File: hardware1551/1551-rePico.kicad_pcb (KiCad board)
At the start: 2 copper layers, 64.1 x 99.4 mm, 37 parts, among them J1 0.96_I2C_OLED, J10 TCBM, J11 JTAG, J6 Conn_01x05, J8 SD CARD, Q1 BSS138, Q2 BSS138, Q3 BSS138, Q4 BSS138, U1 Pico, U3 XC9572XL-VQ64, U4 6523 (pins), U5 6510T (pins), U6 6510T (socket for chip)

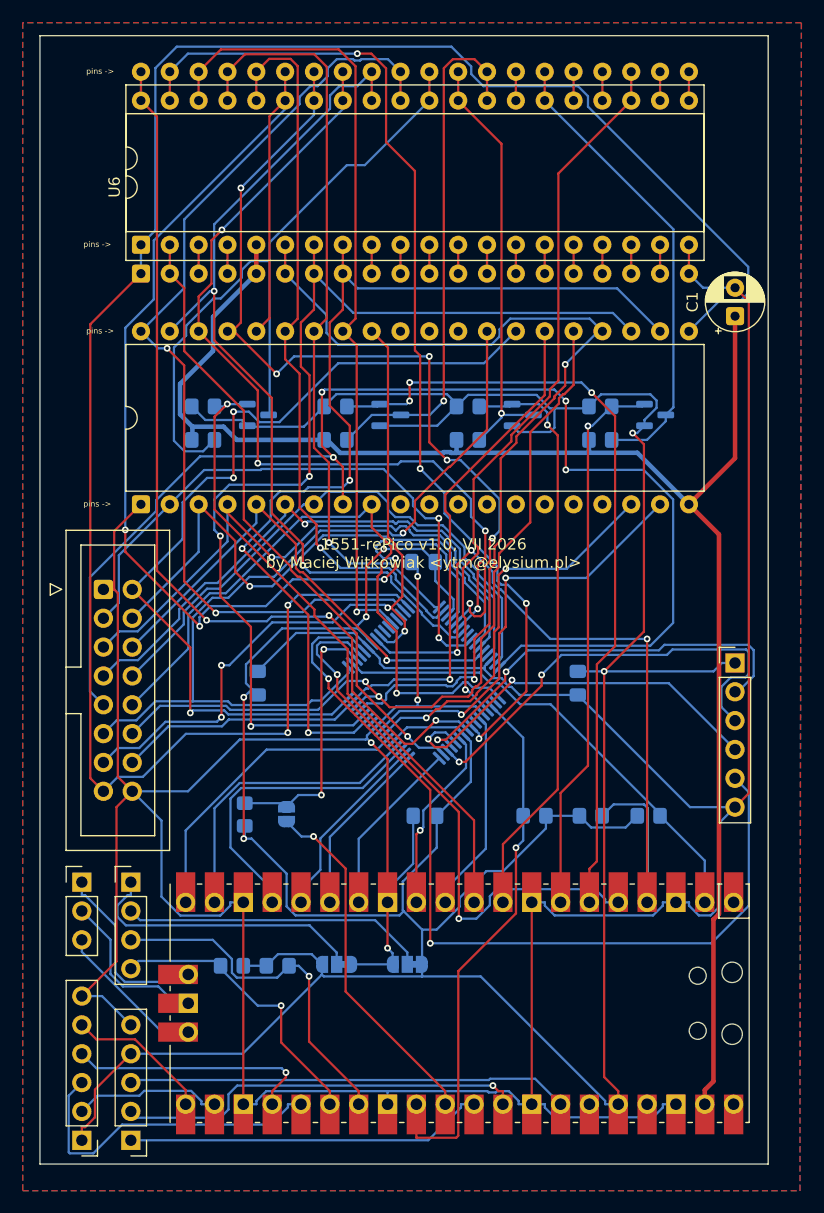
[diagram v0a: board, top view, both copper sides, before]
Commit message: jumpers for future GPIO0/GPIO3 experiments
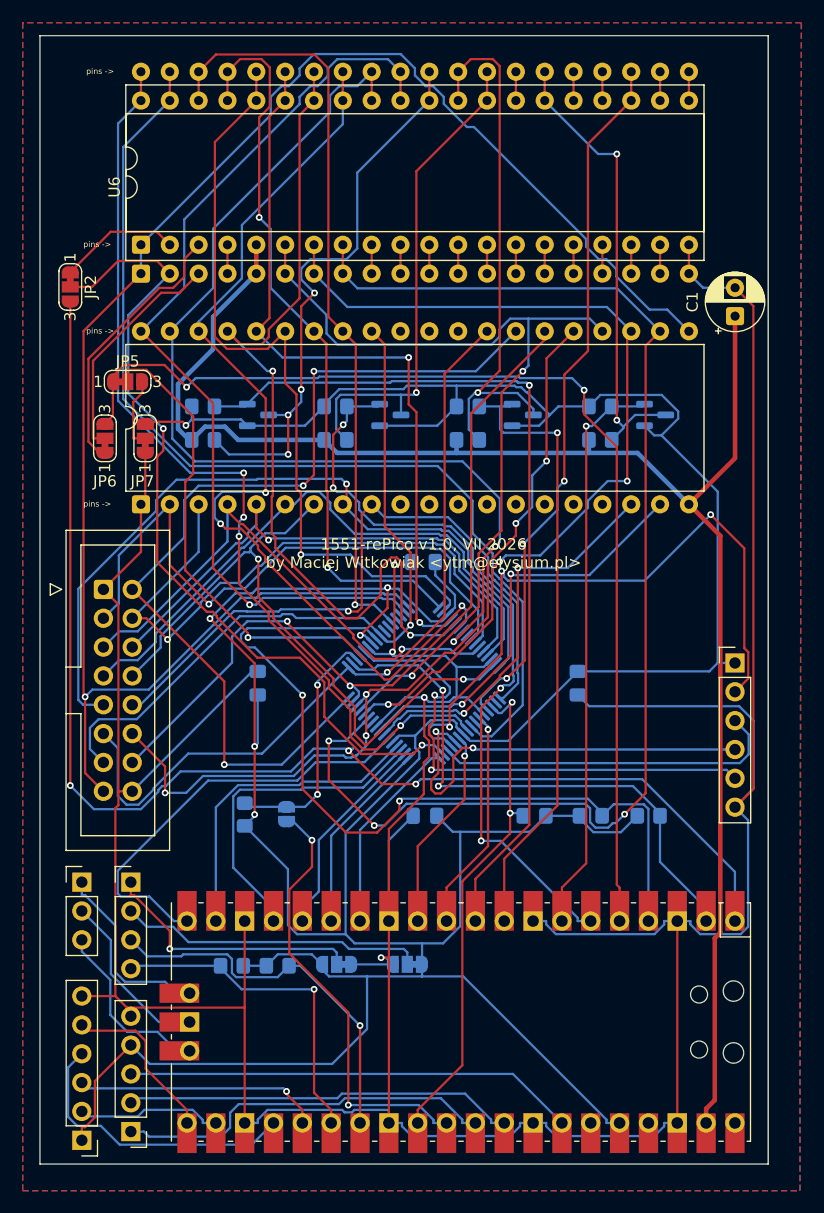
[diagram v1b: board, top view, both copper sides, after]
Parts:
- added JP2: SolderJumper_3_Bridged12, Jumper:SolderJumper-3_P1.3mm_Bridged12_RoundedPad1.0x1.5mm_NumberLabels, F.Cu at (100.8, 85.0)
- added JP5: SolderJumper_3_Bridged12, Jumper:SolderJumper-3_P1.3mm_Bridged12_RoundedPad1.0x1.5mm_NumberLabels, F.Cu at (105.9, 93.3)
- added JP6: SolderJumper_3_Bridged12, Jumper:SolderJumper-3_P1.3mm_Bridged12_RoundedPad1.0x1.5mm_NumberLabels, F.Cu at (103.9, 98.3)
- added JP7: SolderJumper_3_Bridged12, Jumper:SolderJumper-3_P1.3mm_Bridged12_RoundedPad1.0x1.5mm_NumberLabels, F.Cu at (107.4, 98.3)
- moved U1 1.66 mm to (135.2, 149.7)
- moved J6 0.76 mm to (106.1, 159.4)
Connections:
- U1 pad 1: unconnected-(U1-GPIO0-Pad1) -> Net-(JP2-B)
- U1 pad 5: /DEVNUM_3V3 -> Net-(JP5-A)
- U5 pad 2: /PHI0 -> /PHI0_BRD
- U5 pad 3: /~{IRQ} -> /~{IRQ_BRD}
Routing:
- net Net-(JP2-B): track 0.00 -> 114.3 mm, vias 0 -> 3
- net Net-(JP5-A): track 0.00 -> 96.1 mm, vias 0 -> 2
- net /D3: track 115.1 -> 65.2 mm, vias 4 -> 2
- net /DIO7: track 115.2 -> 67.3 mm, vias 4 -> 1
- net /TDO: track 77.2 -> 45.0 mm
- net /~{RESET}: track 178.5 -> 151.8 mm, vias 2 -> 1
- net /A2: track 89.4 -> 114.8 mm
- net /~{IRQ_BRD}: track 0.00 -> 24.0 mm
- net /TMS: track 37.9 -> 59.4 mm, vias 2 -> 3
- net /STP1_3V3: track 56.8 -> 78.0 mm
- net /~{IRQ}: track 2.54 -> 20.4 mm
- net /PHI0: track 55.9 -> 73.3 mm, vias 1 -> 2
- net +3V3: track 331.7 -> 344.1 mm
- net /A1: track 92.2 -> 80.5 mm
- net /STP1: track 62.1 -> 50.4 mm, vias 0 -> 4
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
